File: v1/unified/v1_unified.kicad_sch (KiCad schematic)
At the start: 0 parts

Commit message: feat: impl unified slider
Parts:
- added C1, C3, C5, C8: 0.1uF, symbol Device:C
- added C2, C6: 1uF, symbol Device:C
- added C4, C7: 2.2nF, symbol Device:C
- added E1, E10, E11, E12, E13, E14, E15, E16, E17, E18, E19, E2, E20, E21, E22, E23, E24, E25, E26, E27, E28, E29, E3, E30, E31, E32, E4, E5, E6, E7, E8, E9: Conn_01x01, symbol Connector_Generic:Conn_01x01
- added R1, R10, R11, R12, R13, R14, R15, R16, R17, R18, R19, R2, R20, R21, R22, R23, R24, R25, R26, R27, R28, R29, R3, R30, R31, R32, R4, R5, R6, R7, R8, R9: 560, symbol Device:R
- added R33, R34, R35, R36: 4.7k, symbol Device:R
- added R37, R38, R39, R40: 330, symbol Device:R
- added U1: XIAO-RP2040-SMD, Seeed_Studio_XIAO_Series:XIAO-RP2040-SMD, symbol Seeed_XIAO:XIAO-RP2040-SMD
- added U2, U3: CY8CMBR3116, Package_DFN_QFN:QFN-24-1EP_4x4mm_P0.5mm_EP2.6x2.6mm, symbol Sensor_Touch:CY8CMBR3116
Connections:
- new net: R4.1, U2.4 (CS3)
- new net: E4.1 (Pin_1), R4.2
- new net: E2.1 (Pin_1), R2.2
- new net: R20.1, U3.4 (CS3)
- new net: E20.1 (Pin_1), R20.2
- new net: E17.1 (Pin_1), R17.2
- new net: E22.1 (Pin_1), R22.2
- new net: E12.1 (Pin_1), R12.2
- new net: R25.1, U3.16 (CS8)
- new net: E25.1 (Pin_1), R25.2
- new net: R11.1, U2.14 (CS10)
- new net: E11.1 (Pin_1), R11.2
- new net: E32.1 (Pin_1), R32.2
- new net: C8.1, U3.6 (VCC)
- new net: R18.1, U3.2 (CS1)
- new net: E18.1 (Pin_1), R18.2
- new net: E19.1 (Pin_1), R19.2
- new net: E8.1 (Pin_1), R8.2
- new net: R17.1, U3.1 (CS0)
- new net: R31.1, U3.10 (CS14)
- new net: R30.1, U3.11 (CS13)
- new net: R29.1, U3.12 (CS12)
- new net: R28.1, U3.13 (CS11)
- new net: R27.1, U3.14 (CS10)
- new net: R26.1, U3.15 (CS9)
- new net: R24.1, U3.17 (CS7)
- new net: R23.1, U3.18 (CS6)
- new net: R22.1, U3.19 (CS5)
- new net: R21.1, U3.20 (CS4)
- new net: R33.2, R35.2, R39.1, U2.21 (SDA), U3.21 (SDA)
- new net: R34.2, R36.2, R40.1, U2.22 (SCL), U3.22 (SCL)
- new net: R38.1, U3.24 (~{XRES})
- new net: R19.1, U3.3 (CS2)
- new net: C7.1, U3.5 (CMOD)
- new net: R32.1, U3.9 (CS15)
- new net: R7.1, U2.18 (CS6)
- new net: E7.1 (Pin_1), R7.2
- new net: R2.1, U2.2 (CS1)
- new net: R12.1, U2.13 (CS11)
- new net: E16.1 (Pin_1), R16.2
- new net: E30.1 (Pin_1), R30.2
- new net: C4.1, U2.5 (CMOD)
- new net: R37.1, U2.24 (~{XRES})
- new net: R37.2, U1.1 (D0)
- new net: E10.1 (Pin_1), R10.2
- new net: R13.1, U2.12 (CS12)
- new net: E13.1 (Pin_1), R13.2
- new net: E6.1 (Pin_1), R6.2
- new net: E26.1 (Pin_1), R26.2
- new net: E28.1 (Pin_1), R28.2
- new net: R38.2, U1.2 (D1)
- new net: R14.1, U2.11 (CS13)
- new net: E14.1 (Pin_1), R14.2
- new net: E31.1 (Pin_1), R31.2
- new net: E15.1 (Pin_1), R15.2
- new net: R5.1, U2.20 (CS4)
- new net: E5.1 (Pin_1), R5.2
- new net: C3.1, U2.6 (VCC)
- new net: R3.1, U2.3 (CS2)
- new net: E3.1 (Pin_1), R3.2
- new net: E24.1 (Pin_1), R24.2
- new net: R10.1, U2.15 (CS9)
- new net: R1.1, U2.1 (CS0)
- new net: R15.1, U2.10 (CS14)
- new net: R9.1, U2.16 (CS8)
- new net: R8.1, U2.17 (CS7)
- new net: R6.1, U2.19 (CS5)
- new net: R16.1, U2.9 (CS15)
- new net: E29.1 (Pin_1), R29.2
- new net: E23.1 (Pin_1), R23.2
- new net: E9.1 (Pin_1), R9.2
- new net: E21.1 (Pin_1), R21.2
- new net: R39.2, U1.5 (D4)
- new net: E27.1 (Pin_1), R27.2
- new net: E1.1 (Pin_1), R1.2
- new net: R40.2, U1.6 (D5)
- new net +3V3: C1.1, C2.1, C5.1, C6.1, R33.1, R34.1, R35.1, R36.1, U1.12 (3V3_OUT), U2.7 (VDD), U3.7 (VDD)
- new net GND: C1.2, C2.2, C3.2, C4.2, C5.2, C6.2, C7.2, C8.2, U1.13 (GND), U1.18 (GND), U1.20 (GND), U2.25 (EP), U2.8 (VSS), U3.25 (EP), U3.8 (VSS)
- no-connect marks 0 -> 2

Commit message: fix
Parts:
- removed R39, R40: 330, symbol Device:R
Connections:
- net at R33.2, R35.2, U2.21 (SDA)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: now also R37.1
- net at R34.2, R36.2, U2.22 (SCL)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: now also R38.1
- net at U3.24 (~{XRES}): now also U1.2 (D1); no longer R38.1
- net at U2.24 (~{XRES}): now also U1.1 (D0); no longer R37.1
- net at R37.2: now also U1.5 (D4); no longer U1.1 (D0)
- net at R38.2: now also U1.6 (D5); no longer U1.2 (D1)

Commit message: fix
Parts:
- removed R35, R36: 4.7k, symbol Device:R
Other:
- moved on the sheet: C1, C2, C3, C4, C5, C6, C7, C8, E1, E10, E11, E12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

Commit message: feat: add LED
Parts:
- added C10, C11, C12, C13, C14, C15, C16, C17, C18, C19, C20, C21, C22, C23, C24, C25, C26, C27, C28, C29, C30, C31, C32, C33, C34, C35, C36, C37, C38, C39, C40, C41, C42, C43, C44, C45, C46, C47, C48, C49, C50, C51, C52, C53, C54, C55, C56, C9: 0.1uF, symbol Device:C
- added D1, D10, D11, D12, D13, D14, D15, D16, D17, D18, D19, D2, D20, D21, D22, D23, D24, D25, D26, D27, D28, D29, D3, D30, D31, D32, D33, D34, D35, D36, D37, D38, D39, D4, D40, D41, D42, D43, D44, D45, D46, D47, D48, D5, D6, D7, D8, D9: WS2812B-4020-V6, v1_common:WS2812B-4020-V6, symbol v1_common:WS2812B-4020-V6
- added R35: 330, symbol Device:R
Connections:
- net GND: now also D1.4 (VSS), D10.4 (VSS), D11.4 (VSS), D12.4 (VSS), D13.4 (VSS), D14.4 (VSS), D15.4 (VSS), D16.4 (VSS), D17.4 (VSS), D18.4 (VSS), D19.4 (VSS), D2.4 (VSS), D20.4 (VSS), D21.4 (VSS), D22.4 (VSS), D23.4 (VSS), D24.4 (VSS), D25.4 (VSS), D26.4 (VSS), D27.4 (VSS), D28.4 (VSS), D29.4 (VSS), D3.4 (VSS), D30.4 (VSS), D31.4 (VSS), D32.4 (VSS), D33.4 (VSS), D34.4 (VSS), D35.4 (VSS), D36.4 (VSS), D37.4 (VSS), D38.4 (VSS), D39.4 (VSS), D4.4 (VSS), D40.4 (VSS), D41.4 (VSS), D42.4 (VSS), D43.4 (VSS), D44.4 (VSS), D45.4 (VSS), D46.4 (VSS), D47.4 (VSS), D48.4 (VSS), D5.4 (VSS), D6.4 (VSS), D7.4 (VSS), D8.4 (VSS), D9.4 (VSS)
- net SCL: now reaches R34.2, R38.1, U2.22 (SCL), U3.22 (SCL)
- net SDA: now reaches R33.2, R37.1, U2.21 (SDA), U3.21 (SDA)
- net U3_XRES: now reaches U1.2 (D1), U3.24 (~{XRES})
- net U2_XRES: now reaches U1.1 (D0), U2.24 (~{XRES})
- net at U1.3 (D2): now also R35.2
- new net: C30.2, D22.2 (VDD)
- new net: C33.2, D25.2 (VDD)
- new net: D42.3 (DOUT), D43.1 (DIN)
- new net: C51.2, D43.2 (VDD)
- new net: D43.3 (DOUT), D44.1 (DIN)
- new net: D13.3 (DOUT), D14.1 (DIN)
- new net: C22.2, D14.2 (VDD)
- new net: D14.3 (DOUT), D15.1 (DIN)
- new net: D5.3 (DOUT), D6.1 (DIN)
- new net: C14.2, D6.2 (VDD)
- new net: D6.3 (DOUT), D7.1 (DIN)
- new net: D10.3 (DOUT), D11.1 (DIN)
- new net: C19.2, D11.2 (VDD)
- new net: D11.3 (DOUT), D12.1 (DIN)
- new net: C25.2, D17.2 (VDD)
- new net: C41.2, D33.2 (VDD)
- new net: C17.2, D9.2 (VDD)
- new net: D10.1 (DIN), D9.3 (DOUT)
- new net: C18.2, D10.2 (VDD)
- new net: D21.3 (DOUT), D22.1 (DIN)
- new net: D22.3 (DOUT), D23.1 (DIN)
- new net: C45.2, D37.2 (VDD)
- new net: C46.2, D38.2 (VDD)
- new net: C21.2, D13.2 (VDD)
- new net: C12.2, D4.2 (VDD)
- new net: D33.3 (DOUT), D34.1 (DIN)
- new net: C42.2, D34.2 (VDD)
- new net: D34.3 (DOUT), D35.1 (DIN)
- new net: D41.3 (DOUT), D42.1 (DIN)
- new net: C50.2, D42.2 (VDD)
- new net: C23.2, D15.2 (VDD)
- new net: C37.2, D29.2 (VDD)
- new net: C32.2, D24.2 (VDD)
- new net: D17.3 (DOUT), D18.1 (DIN)
- new net: C20.2, D12.2 (VDD)
- new net: C11.2, D3.2 (VDD)
- new net: C43.2, D35.2 (VDD)
- new net: D35.3 (DOUT), D36.1 (DIN)
- new net: C48.2, D40.2 (VDD)
- new net: D19.3 (DOUT), D20.1 (DIN)
- new net: C28.2, D20.2 (VDD)
- new net: D20.3 (DOUT), D21.1 (DIN)
- new net: C44.2, D36.2 (VDD)
- new net: D36.3 (DOUT), D37.1 (DIN)
- new net: C53.2, D45.2 (VDD)
- new net: C36.2, D28.2 (VDD)
- new net: C38.2, D30.2 (VDD)
- new net: D37.3 (DOUT), D38.1 (DIN)
- new net: C55.2, D47.2 (VDD)
- new net: D1.3 (DOUT), D2.1 (DIN)
- new net: C10.2, D2.2 (VDD)
- new net: D2.3 (DOUT), D3.1 (DIN)
- new net: C31.2, D23.2 (VDD)
- new net: D15.3 (DOUT), D16.1 (DIN)
- new net: D45.3 (DOUT), D46.1 (DIN)
- new net: C54.2, D46.2 (VDD)
- new net: D46.3 (DOUT), D47.1 (DIN)
- new net: D8.3 (DOUT), D9.1 (DIN)
- new net: C49.2, D41.2 (VDD)
- new net: D7.3 (DOUT), D8.1 (DIN)
- new net: C16.2, D8.2 (VDD)
- new net: C39.2, D31.2 (VDD)
- new net: C35.2, D27.2 (VDD)
- new net: D31.3 (DOUT), D32.1 (DIN)
- new net: C40.2, D32.2 (VDD)
- new net: D47.3 (DOUT), D48.1 (DIN)
- new net: C56.2, D48.2 (VDD)
- new net: D27.3 (DOUT), D28.1 (DIN)
- new net: D28.3 (DOUT), D29.1 (DIN)
- new net: D3.3 (DOUT), D4.1 (DIN)
- new net: D4.3 (DOUT), D5.1 (DIN)
- new net: D12.3 (DOUT), D13.1 (DIN)
- new net: D38.3 (DOUT), D39.1 (DIN)
- new net: C47.2, D39.2 (VDD)
- new net: D39.3 (DOUT), D40.1 (DIN)
- new net: C15.2, D7.2 (VDD)
- new net: D23.3 (DOUT), D24.1 (DIN)
- new net: C29.2, D21.2 (VDD)
- new net: D25.3 (DOUT), D26.1 (DIN)
- new net: C34.2, D26.2 (VDD)
- new net: D26.3 (DOUT), D27.1 (DIN)
- new net: C9.2, D1.2 (VDD)
- new net: C24.2, D16.2 (VDD)
- new net: D30.3 (DOUT), D31.1 (DIN)
- new net: D29.3 (DOUT), D30.1 (DIN)
- new net: C27.2, D19.2 (VDD)
- new net: C13.2, D5.2 (VDD)
- new net: D44.3 (DOUT), D45.1 (DIN)
- new net: C26.2, D18.2 (VDD)
- new net: D18.3 (DOUT), D19.1 (DIN)
- new net: D24.3 (DOUT), D25.1 (DIN)
- new net: C52.2, D44.2 (VDD)
- new net LED_5V: C10.1, C11.1, C12.1, C13.1, C14.1, C15.1, C16.1, C17.1, C18.1, C19.1, C20.1, C21.1, C22.1, C23.1, C24.1, C25.1, C26.1, C27.1, C28.1, C29.1, C30.1, C31.1, C32.1, C33.1, C34.1, C35.1, C36.1, C37.1, C38.1, C39.1, C40.1, C41.1, C42.1, C43.1, C44.1, C45.1, C46.1, C47.1, C48.1, C49.1, C50.1, C51.1, C52.1, C53.1, C54.1, C55.1, C56.1, C9.1
- new net LED_DIN1: D1.1 (DIN), R35.1
- new net LED_DIN2: D16.3 (DOUT), D17.1 (DIN)
- new net LED_DIN3: D32.3 (DOUT), D33.1 (DIN)
- new net LED_DIN4: D40.3 (DOUT), D41.1 (DIN)
- no-connect marks 2 -> 3
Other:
- moved on the sheet: C1, C2, C3, C4, C7, E1, E10, E11, E12, E13, E14, E15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

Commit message: feat: add LED
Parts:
- added C57: 100uF, symbol Device:C
- added J33: USB_C_Receptacle_PowerOnly_6P, symbol Connector:USB_C_Receptacle_PowerOnly_6P
- added R38, R39: 5.1k, symbol Device:R
- renumbered E1 to J1, E10 to J10, E11 to J11, E12 to J12, E13 to J13, E14 to J14, E15 to J15, E16 to J16, E17 to J17, E18 to J18, E19 to J19, E2 to J2, E20 to J20, E21 to J21, E22 to J22, E23 to J23, E24 to J24, E25 to J25, E26 to J26, E27 to J27, E28 to J28, E29 to J29, E3 to J3, E30 to J30, E31 to J31, E32 to J32, E4 to J4, E5 to J5, E6 to J6, E7 to J7, E8 to J8, E9 to J9, R37 to R36, R38 to R37
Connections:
- net GND: now also C10.2, C11.2, C12.2, C13.2, C14.2, C15.2, C16.2, C17.2, C18.2, C19.2, C20.2, C21.2, C22.2, C23.2, C24.2, C25.2, C26.2, C27.2, C28.2, C29.2, C30.2, C31.2, C32.2, C33.2, C34.2, C35.2, C36.2, C37.2, C38.2, C39.2, C40.2, C41.2, C42.2, C43.2, C44.2, C45.2, C46.2, C47.2, C48.2, C49.2, C50.2, C51.2, C52.2, C53.2, C54.2, C55.2, C56.2, C9.2, C57.2, J33.A12 (GND), J33.B12 (GND), J33.SH (SHIELD), R38.2, R39.2
- net LED_5V: now also D1.2 (VDD), D10.2 (VDD), D11.2 (VDD), D12.2 (VDD), D13.2 (VDD), D14.2 (VDD), D15.2 (VDD), D16.2 (VDD), D17.2 (VDD), D18.2 (VDD), D19.2 (VDD), D2.2 (VDD), D20.2 (VDD), D21.2 (VDD), D22.2 (VDD), D23.2 (VDD), D24.2 (VDD), D25.2 (VDD), D26.2 (VDD), D27.2 (VDD), D28.2 (VDD), D29.2 (VDD), D3.2 (VDD), D30.2 (VDD), D31.2 (VDD), D32.2 (VDD), D33.2 (VDD), D34.2 (VDD), D35.2 (VDD), D36.2 (VDD), D37.2 (VDD), D38.2 (VDD), D39.2 (VDD), D4.2 (VDD), D40.2 (VDD), D41.2 (VDD), D42.2 (VDD), D43.2 (VDD), D44.2 (VDD), D45.2 (VDD), D46.2 (VDD), D47.2 (VDD), D48.2 (VDD), D5.2 (VDD), D6.2 (VDD), D7.2 (VDD), D8.2 (VDD), D9.2 (VDD), C57.1, J33.A9 (VBUS), J33.B9 (VBUS)
- new net: J33.A5 (CC1), R39.1
- new net: J33.B5 (CC2), R38.1
- no-connect marks 3 -> 9
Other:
- moved on the sheet: C1, C2, C27, C28, C29, C3, C30, C31, C32, C33, C34, C35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

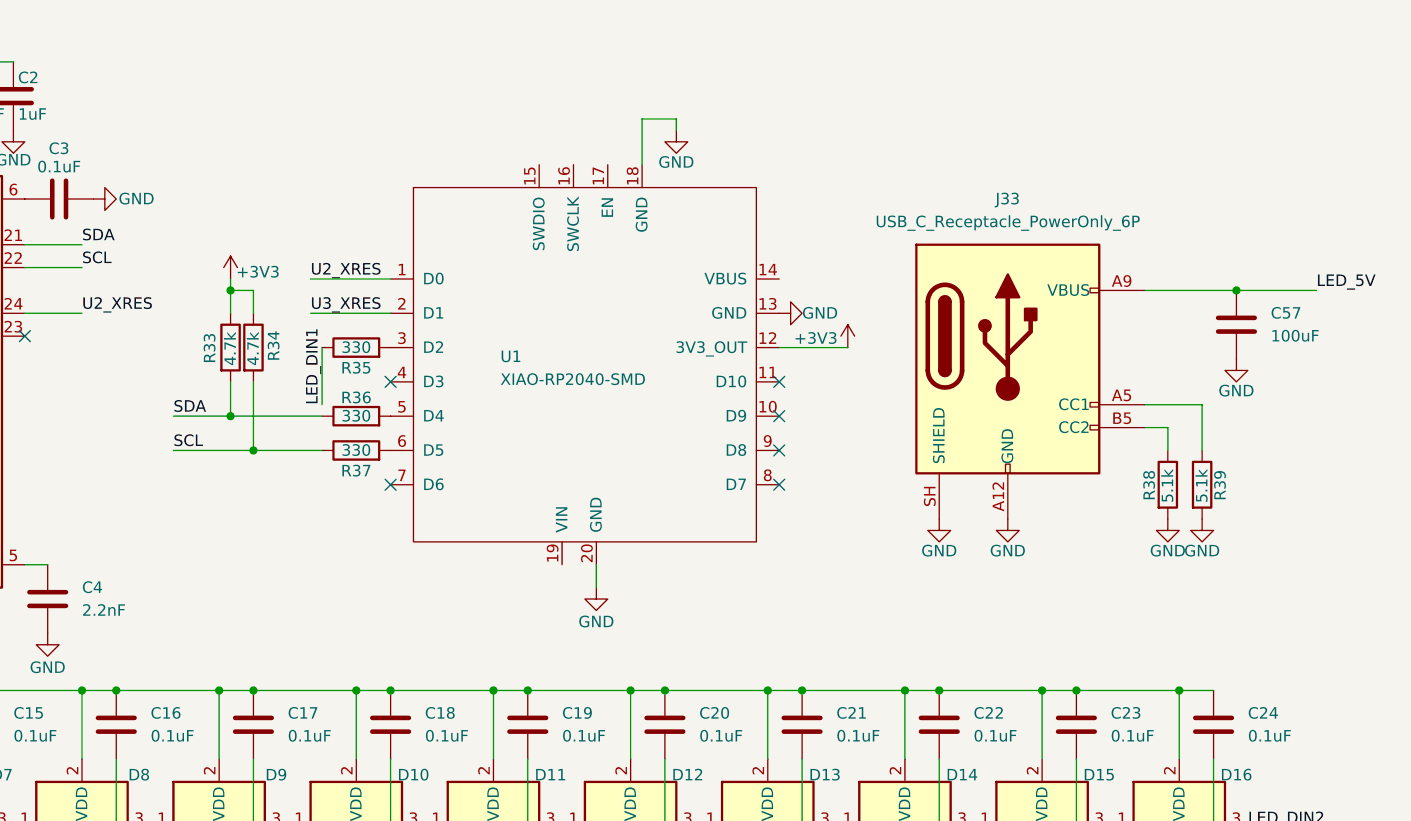
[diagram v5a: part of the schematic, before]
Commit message: feat: Pico にする＆DCジャックから電源を取るように
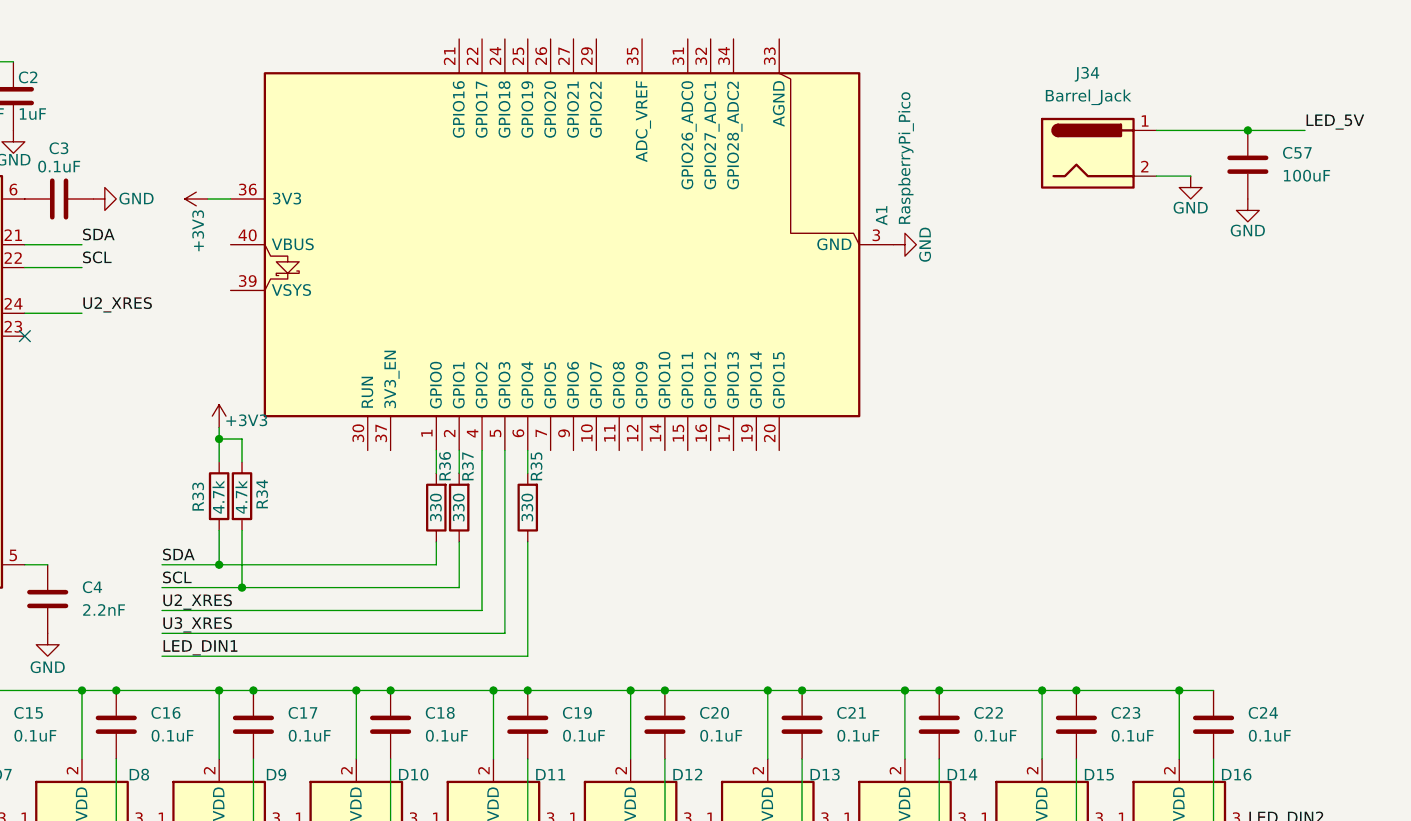
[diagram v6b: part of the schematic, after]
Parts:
- removed J33: USB_C_Receptacle_PowerOnly_6P, symbol Connector:USB_C_Receptacle_PowerOnly_6P
- removed R38, R39: 5.1k, symbol Device:R
- removed U1: XIAO-RP2040-SMD, Seeed_Studio_XIAO_Series:XIAO-RP2040-SMD, symbol Seeed_XIAO:XIAO-RP2040-SMD
- added A1: RaspberryPi_Pico, Module:RaspberryPi_Pico_Common_Unspecified, symbol MCU_Module:RaspberryPi_Pico
- added J34: Barrel_Jack, symbol Connector:Barrel_Jack
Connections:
- net +3V3: now also A1.36 (3V3)
- net GND: now also A1.13 (GND), A1.18 (GND), A1.23 (GND), A1.28 (GND), A1.3 (GND), A1.38 (GND), A1.8 (GND), J34.2
- net LED_5V: now also J34.1
- net U2_XRES: now also A1.4 (GPIO2)
- net U3_XRES: now also A1.5 (GPIO3)
- net at R37.2: now also A1.2 (GPIO1)
- net at R35.2: now also A1.6 (GPIO4)
- net at R36.2: now also A1.1 (GPIO0)
- no-connect marks 9 -> 3

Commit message: fix
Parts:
- removed C57: 100uF, symbol Device:C
- added C57: 100uF, symbol Device:C_Polarized
- added J34, J35, J36, J37: Conn_01x04, symbol Connector_Generic:Conn_01x04
- added Q1, Q2, Q3, Q4: 2N7002, Package_TO_SOT_SMD:SOT-23, symbol Transistor_FET:2N7002
- added R38, R39, R40, R41: 100k, symbol Device:R
- renumbered J34 to J33
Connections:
- net GND: now also C57.2, J34.4 (Pin_4), J35.4 (Pin_4), J36.4 (Pin_4), J37.4 (Pin_4), Q1.2 (S), Q2.2 (S), Q3.2 (S), Q4.2 (S), R38.2, R39.2, R40.2, R41.2
- net LED_5V: now also C57.1
- net LED_DIN2: now also D24.3 (DOUT), D25.1 (DIN); no longer D16.3 (DOUT), D17.1 (DIN)
- net at A1.10 (GPIO7): now also J36.3 (Pin_3)
- net at A1.11 (GPIO8): now also J37.3 (Pin_3)
- net at A1.12 (GPIO9): now also Q1.1 (G), R38.1
- net at A1.14 (GPIO10): now also Q2.1 (G), R39.1
- net at A1.15 (GPIO11): now also Q3.1 (G), R40.1
- net at A1.16 (GPIO12): now also Q4.1 (G), R41.1
- net BUTTON_5V: now reaches A1.40 (VBUS)
- net BUTTON_5V: now also J34.1 (Pin_1), J35.1 (Pin_1), J36.1 (Pin_1), J37.1 (Pin_1)
- net at A1.7 (GPIO5): now also J34.3 (Pin_3)
- net at A1.9 (GPIO6): now also J35.3 (Pin_3)
- net LED_DIN3: no longer names the net of D32.3 (DOUT), D33.1 (DIN)
- net LED_DIN4: no longer names the net of D40.3 (DOUT), D41.1 (DIN)
- new net: J35.2 (Pin_2), Q2.3 (D)
- new net: J36.2 (Pin_2), Q3.3 (D)
- new net: J34.2 (Pin_2), Q1.3 (D)
- new net: D16.3 (DOUT), D17.1 (DIN)
- new net: J37.2 (Pin_2), Q4.3 (D)
- no-connect marks 3 -> 21
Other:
- moved on the sheet: A1, C1, C10, C11, C12, C13, C14, C15, C16, C17, C18, C19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

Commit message: fix
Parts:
- added C58: 0.1uF, symbol Device:C
- added R42: 100k, symbol Device:R
- added U1: 74AHCT1G125, symbol 74xGxx:74AHCT1G125
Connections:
- net GND: now also C58.2, R42.2, U1.1, U1.3 (GND)
- net LED_5V: now also C58.1, U1.5 (VCC)
- net at A1.6 (GPIO4): now also R42.1, U1.2; no longer R35.2
- new net: R35.2, U1.4
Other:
- moved on the sheet: R35
